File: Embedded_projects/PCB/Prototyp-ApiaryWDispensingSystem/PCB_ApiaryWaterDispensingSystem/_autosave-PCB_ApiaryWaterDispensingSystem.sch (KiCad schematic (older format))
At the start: 0 parts

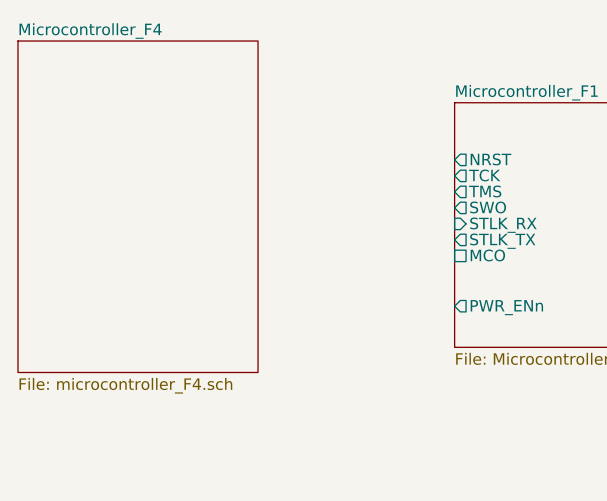
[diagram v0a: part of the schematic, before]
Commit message: added changes of Microntroller_F4 ->global variables #3
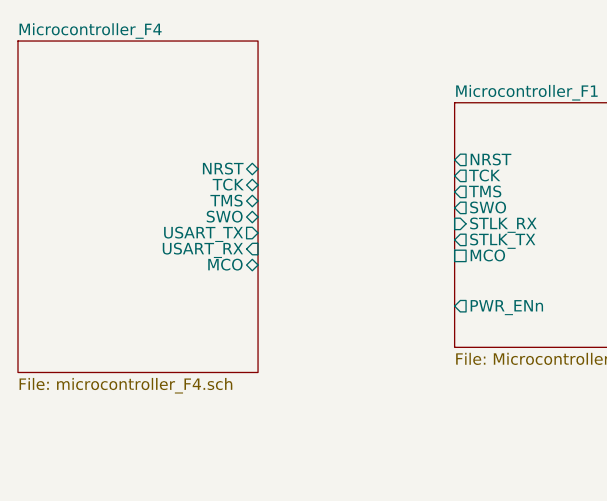
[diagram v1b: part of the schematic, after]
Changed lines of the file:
@@
 F0 "Microcontroller_F4" 50
 F1 "microcontroller_F4.sch" 50
+F2 "SWO" B R 2230 2180 50
+F3 "USART_TX" O R 2230 2250 50
+F4 "USART_RX" I R 2230 2320 50
+F5 "TMS" B R 2230 2110 50
+F6 "TCK" B R 2230 2040 50
+F7 "MCO" B R 2230 2390 50
+F8 "NRST" B R 2230 1970 50
 $EndSheet
 $Sheet
